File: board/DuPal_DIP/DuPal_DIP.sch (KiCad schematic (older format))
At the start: 45 parts, among them J1 AVR-ISP-6, J2 RS232, J3 Power IN, SW1 SW_Push, SW2 Power, U1 ATmega8A-PU, U2 74HC595, U3 74HC595, U5 20 Pin PAL, U6 MAX232, U7 L7805, Y1 8Mhz

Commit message: Begin connecting the new ICs in the circuit
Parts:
- removed U?: FT232RL, Package_SO:SSOP-28_5.3x10.2mm_P0.65mm, symbol Interface_USB:FT232RL
- added C? (x3): 100nF, Capacitor_THT:C_Disc_D3.4mm_W2.1mm_P2.50mm, symbol Device:C_Small
- added D?: PAL24_LED, LED_THT:LED_D2.0mm_W4.8mm_H2.5mm_FlatTop, symbol Device:LED_Small
- added D?: PAL20_LED, LED_THT:LED_D2.0mm_W4.8mm_H2.5mm_FlatTop, symbol Device:LED_Small
- added R? (x2): 680, Resistor_THT:R_Axial_DIN0204_L3.6mm_D1.6mm_P7.62mm_Horizontal, symbol Device:R_Small
- R16: value 470 -> 680
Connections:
- net labels added: PISO_I_1, PISO_I_10, PISO_I_11, PISO_I_12, PISO_I_13, PISO_I_14, PISO_I_15, PISO_I_16, PISO_I_2, PISO_I_3, PISO_I_4, PISO_I_5, PISO_I_6, PISO_I_7, PISO_I_8, PISO_I_9
- wire segments 298 -> 324
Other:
- moved on the sheet: C10, C11, C12, C8, C9, R1, R2, R3, R4, R5, R6, R7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

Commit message: Add 24 pin slot
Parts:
- added U?: 24 Pin PAL, symbol Logic_Programmable:PAL20L8
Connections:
- net labels added: P24_1, P24_10, P24_11, P24_13, P24_14, P24_15, P24_16, P24_17, P24_18, P24_19, P24_2, P24_20, P24_21, P24_22, P24_23, P24_3, P24_4, P24_5, P24_6, P24_7, P24_8, P24_9
- wire segments 324 -> 348
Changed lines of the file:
@@
 L Logic_Programmable:PAL16L8 U5
 U 1 1 5E5512FA
-P 6700 1650
-F 0 "U5" H 6400 2250 50  0000 C CNN
-F 1 "20 Pin PAL" H 6950 2250 50  0000 C CNN
-F 2 "Socket:DIP_Socket-20_W4.3_W5.08_W7.62_W10.16_W10.9_3M_220-3342-00-0602J" H 6700 1650 50  0001 C CNN
-F 3 "" H 6700 1650 50  0001 C CNN
-	1    6700 1650
+P 6300 1550
+F 0 "U5" H 6000 2150 50  0000 C CNN
+F 1 "20 Pin PAL" H 6550 2150 50  0000 C CNN
+F 2 "Socket:DIP_Socket-20_W4.3_W5.08_W7.62_W10.16_W10.9_3M_220-3342-00-0602J" H 6300 1550 50  0001 C CNN
+F 3 "" H 6300 1550 50  0001 C CNN
+	1    6300 1550
 	1    0    0    -1
 $EndComp
@@
 L power:GND #PWR0104
 U 1 1 5E551F7F
-P 6700 2300
-F 0 "#PWR0104" H 6700 2050 50  0001 C CNN
-F 1 "GND" H 6705 2127 50  0000 C CNN
-F 2 "" H 6700 2300 50  0001 C CNN
-F 3 "" H 6700 2300 50  0001 C CNN
-	1    6700 2300
-	1    0    0    -1
-$EndComp
-Wire Wire Line
-	6700 2300 6700 2250
+P 6300 2200
+F 0 "#PWR0104" H 6300 1950 50  0001 C CNN
+F 1 "GND" H 6305 2027 50  0000 C CNN
+F 2 "" H 6300 2200 50  0001 C CNN
+F 3 "" H 6300 2200 50  0001 C CNN
+	1    6300 2200
+	1    0    0    -1
+$EndComp
+Wire Wire Line
+	6300 2200 6300 2150
 $Comp
 L power:VCC #PWR0105
 U 1 1 5E5538C6
-P 6700 900
-F 0 "#PWR0105" H 6700 750 50  0001 C CNN
-F 1 "VCC" H 6717 1073 50  0000 C CNN
-F 2 "" H 6700 900 50  0001 C CNN
-F 3 "" H 6700 900 50  0001 C CNN
-	1    6700 900
-	1    0    0    -1
-$EndComp
-Wire Wire Line
-	6700 900  6700 950
+P 6300 800
+F 0 "#PWR0105" H 6300 650 50  0001 C CNN
+F 1 "VCC" H 6317 973 50  0000 C CNN
+F 2 "" H 6300 800 50  0001 C CNN
+F 3 "" H 6300 800 50  0001 C CNN
+	1    6300 800
+	1    0    0    -1
+$EndComp
+Wire Wire Line
+	6300 800  6300 850
 $Comp
 L power:VCC #PWR0106
@@
 P20_19
 Wire Wire Line
-	6200 1150 5750 1150
-Wire Wire Line
-	6200 1250 5750 1250
-Wire Wire Line
-	6200 1350 5750 1350
-Wire Wire Line
-	6200 1450 5750 1450
-Wire Wire Line
-	6200 1550 5750 1550
-Wire Wire Line
-	6200 1650 5750 1650
-Wire Wire Line
-	6200 1750 5750 1750
-Wire Wire Line
-	6200 1850 5750 1850
-Wire Wire Line
-	6200 1950 5750 1950
-Wire Wire Line
-	6200 2050 5750 2050
-Wire Wire Line
-	7200 1150 7800 1150
-Wire Wire Line
-	7200 1250 7800 1250
-Wire Wire Line
-	7200 1350 7800 1350
-Wire Wire Line
-	7200 1450 7800 1450
-Wire Wire Line
-	7200 1550 7800 1550
-Wire Wire Line
-	7200 1650 7800 1650
-Wire Wire Line
-	7200 1750 7800 1750
-Wire Wire Line
-	7200 1850 7800 1850
-Text Label 5750 1150 0    50   ~ 0
+	5800 1050 5350 1050
+Wire Wire Line
+	5800 1150 5350 1150
+Wire Wire Line
+	5800 1250 5350 1250
+Wire Wire Line
+	5800 1350 5350 1350
+Wire Wire Line
+	5800 1450 5350 1450
+Wire Wire Line
+	5800 1550 5350 1550
+Wire Wire Line
+	5800 1650 5350 1650
+Wire Wire Line
+	5800 1750 5350 1750
+Wire Wire Line
+	5800 1850 5350 1850
+Wire Wire Line
+	5800 1950 5350 1950
+Wire Wire Line
+	6800 1050 7400 1050
+Wire Wire Line
+	6800 1150 7400 1150
+Wire Wire Line
+	6800 1250 7400 1250
+Wire Wire Line
+	6800 1350 7400 1350
+Wire Wire Line
+	6800 1450 7400 1450
+Wire Wire Line
+	6800 1550 7400 1550
+Wire Wire Line
+	6800 1650 7400 1650
+Wire Wire Line
+	6800 1750 7400 1750
+Text Label 5350 1050 0    50   ~ 0
 P20_1
-Text Label 5750 1250 0    50   ~ 0
+Text Label 5350 1150 0    50   ~ 0
 P20_2
-Text Label 5750 1350 0    50   ~ 0
+Text Label 5350 1250 0    50   ~ 0
 P20_3
-Text Label 5750 1450 0    50   ~ 0
+Text Label 5350 1350 0    50   ~ 0
 P20_4
-Text Label 5750 1550 0    50   ~ 0
+Text Label 5350 1450 0    50   ~ 0
 P20_5
-Text Label 5750 1650 0    50   ~ 0
+Text Label 5350 1550 0    50   ~ 0
 P20_6
-Text Label 5750 1750 0    50   ~ 0
+Text Label 5350 1650 0    50   ~ 0
 P20_7
-Text Label 5750 1850 0    50   ~ 0
+Text Label 5350 1750 0    50   ~ 0
 P20_8
-Text Label 5750 1950 0    50   ~ 0
+Text Label 5350 1850 0    50   ~ 0
 P20_9
-Text Label 5750 2050 0    50   ~ 0
+Text Label 5350 1950 0    50   ~ 0
 P20_11
-Text Label 7800 1850 2    50   ~ 0
+Text Label 7400 1750 2    50   ~ 0
 P20_12
-Text Label 7800 1750 2    50   ~ 0
+Text Label 7400 1650 2    50   ~ 0
 P20_13
-Text Label 7800 1650 2    50   ~ 0
+Text Label 7400 1550 2    50   ~ 0
 P20_14
-Text Label 7800 1550 2    50   ~ 0
+Text Label 7400 1450 2    50   ~ 0
 P20_15
-Text Label 7800 1450 2    50   ~ 0
+Text Label 7400 1350 2    50   ~ 0
 P20_16
-Text Label 7800 1350 2    50   ~ 0
+Text Label 7400 1250 2    50   ~ 0
 P20_17
-Text Label 7800 1250 2    50   ~ 0
+Text Label 7400 1150 2    50   ~ 0
 P20_18
-Text Label 7800 1150 2    50   ~ 0
+Text Label 7400 1050 2    50   ~ 0
 P20_19
 NoConn ~ 14350 5800
@@
 Wire Wire Line
 	4150 2550 4150 2600
+$Comp
+L Logic_Programmable:PAL20L8 U?
+U 1 1 61C8AE16
+P 8500 1750
+F 0 "U?" H 8200 2550 50  0000 C CNN
+F 1 "24 Pin PAL" H 8750 2550 50  0000 C CNN
+F 2 "" H 8500 1750 50  0001 C CNN
+F 3 "" H 8500 1750 50  0001 C CNN
+	1    8500 1750
+	1    0    0    -1
+$EndComp
+$Comp
+L power:VCC #PWR?
+U 1 1 61D2E65D
+P 8500 800
+F 0 "#PWR?" H 8500 650 50  0001 C CNN
+F 1 "VCC" H 8517 973 50  0000 C CNN
+F 2 "" H 8500 800 50  0001 C CNN
+F 3 "" H 8500 800 50  0001 C CNN
+	1    8500 800
+	1    0    0    -1
+$EndComp
+Wire Wire Line
+	8500 800  8500 850
+$Comp
+L power:GND #PWR?
+U 1 1 61D50A38
+P 8500 2600
+F 0 "#PWR?" H 8500 2350 50  0001 C CNN
+F 1 "GND" H 8505 2427 50  0000 C CNN
+F 2 "" H 8500 2600 50  0001 C CNN
+F 3 "" H 8500 2600 50  0001 C CNN
+	1    8500 2600
+	1    0    0    -1
+$EndComp
+Wire Wire Line
+	8500 2550 8500 2600
+Wire Wire Line
+	8000 1050 7600 1050
+Wire Wire Line
+	8000 1150 7600 1150
+Wire Wire Line
+	8000 1250 7600 1250
+Wire Wire Line
+	8000 1350 7600 1350
+Wire Wire Line
+	8000 1450 7600 1450
+Wire Wire Line
+	8000 1550 7600 1550
+Wire Wire Line
+	8000 1650 7600 1650
+Wire Wire Line
+	8000 1750 7600 1750
+Wire Wire Line
+	8000 1850 7600 1850
+Wire Wire Line
+	8000 1950 7600 1950
+Wire Wire Line
+	8000 2050 7600 2050
+Wire Wire Line
+	8000 2150 7600 2150
+Wire Wire Line
+	8000 2250 7600 2250
+Wire Wire Line
+	8000 2350 7600 2350
+Wire Wire Line
+	9000 1050 9400 1050
+Wire Wire Line
+	9000 1150 9400 1150
+Wire Wire Line
+	9000 1250 9400 1250
+Wire Wire Line
+	9000 1350 9400 1350
+Wire Wire Line
+	9000 1450 9400 1450
+Wire Wire Line
+	9000 1550 9400 1550
+Wire Wire Line
+	9000 1650 9400 1650
+Wire Wire Line
+	9000 1750 9400 1750
+Text Label 7600 1050 0    50   ~ 0
+P24_1
+Text Label 7600 1150 0    50   ~ 0
+P24_2
+Text Label 7600 1250 0    50   ~ 0
+P24_3
+Text Label 7600 1350 0    50   ~ 0
+P24_4
+Text Label 7600 1450 0    50   ~ 0
+P24_5
+Text Label 7600 1550 0    50   ~ 0
+P24_6
+Text Label 7600 1650 0    50   ~ 0
+P24_7
+Text Label 7600 1750 0    50   ~ 0
+P24_8
+Text Label 7600 1850 0    50   ~ 0
+P24_9
+Text Label 7600 1950 0    50   ~ 0
+P24_10
+Text Label 7600 2050 0    50   ~ 0
+P24_11
+Text Label 7600 2150 0    50   ~ 0
+P24_13
+Text Label 7600 2250 0    50   ~ 0
+P24_14
+Text Label 7600 2350 0    50   ~ 0
+P24_23
+Text Label 9400 1750 2    50   ~ 0
+P24_15
+Text Label 9400 1650 2    50   ~ 0
+P24_16
+Text Label 9400 1550 2    50   ~ 0
+P24_17
+Text Label 9400 1450 2    50   ~ 0
+P24_18
+Text Label 9400 1350 2    50   ~ 0
+P24_19
+Text Label 9400 1250 2    50   ~ 0
+P24_20
+Text Label 9400 1150 2    50   ~ 0
+P24_21
+Text Label 9400 1050 2    50   ~ 0
+P24_22
 $EndSCHEMATC

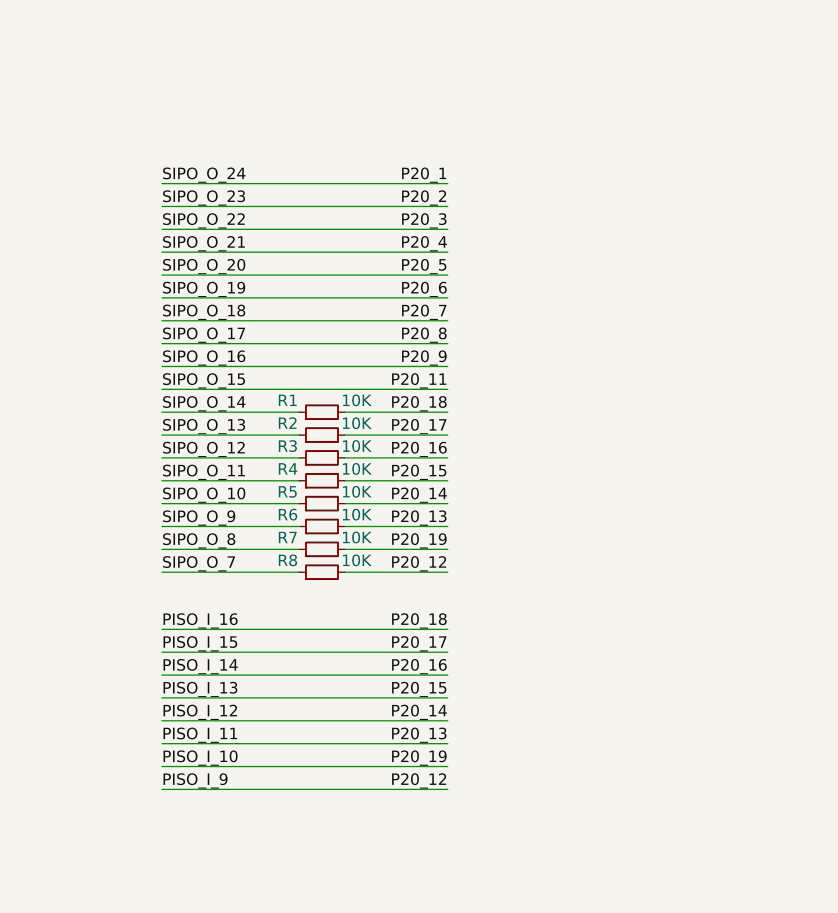
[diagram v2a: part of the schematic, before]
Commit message: Connected both PAL outputs
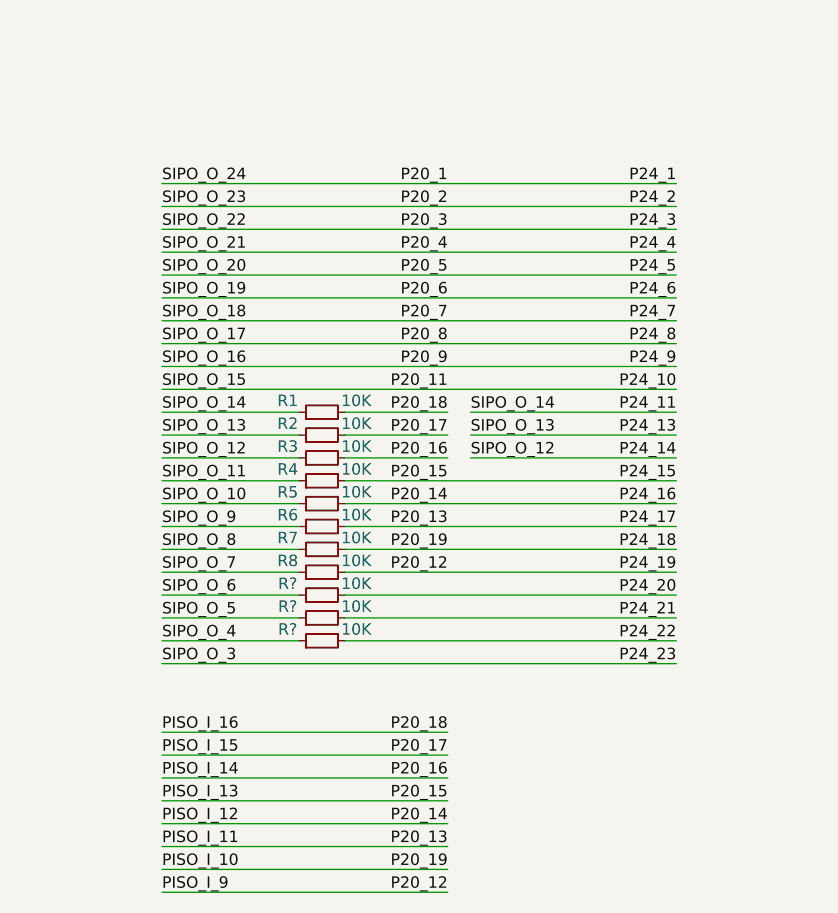
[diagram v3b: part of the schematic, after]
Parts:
- added R? (x3): 10K, Resistor_THT:R_Axial_DIN0204_L3.6mm_D1.6mm_P7.62mm_Horizontal, symbol Device:R_Small
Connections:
- wire segments 348 -> 358
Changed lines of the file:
@@
 Text Label 12500 5350 2    50   ~ 0
 PISO_SER
-Wire Wire Line
-	8500 6350 9750 6350
-Wire Wire Line
-	8500 6450 9750 6450
-Wire Wire Line
-	8500 6550 9750 6550
-Wire Wire Line
-	8500 6650 9750 6650
-Wire Wire Line
-	8500 6750 9750 6750
-Wire Wire Line
-	8500 6850 9750 6850
-Wire Wire Line
-	8500 6950 9750 6950
-Wire Wire Line
-	8500 7050 9750 7050
-Wire Wire Line
-	8500 7150 9750 7150
-Wire Wire Line
-	8500 7250 9750 7250
 Text Label 9750 6350 2    50   ~ 0
 P20_1
@@
 	9300 7550 9750 7550
 Wire Wire Line
-	9300 7650 9750 7650
-Wire Wire Line
-	9300 7750 9750 7750
-Wire Wire Line
-	9300 7850 9750 7850
-Wire Wire Line
-	9300 7950 9750 7950
-Wire Wire Line
-	9300 8050 9750 8050
-Wire Wire Line
 	8500 7350 9100 7350
 Wire Wire Line
@@
 PISO_I_16
 Wire Wire Line
-	8500 8300 9750 8300
-Wire Wire Line
-	8500 8400 9750 8400
-Wire Wire Line
-	8500 8500 9750 8500
-Wire Wire Line
-	8500 8600 9750 8600
-Wire Wire Line
-	8500 8700 9750 8700
-Wire Wire Line
-	8500 8800 9750 8800
-Wire Wire Line
-	8500 8900 9750 8900
-Wire Wire Line
-	8500 9000 9750 9000
-Text Label 9750 8900 2    50   ~ 0
+	8500 8750 9750 8750
+Wire Wire Line
+	8500 8850 9750 8850
+Wire Wire Line
+	8500 8950 9750 8950
+Wire Wire Line
+	8500 9050 9750 9050
+Wire Wire Line
+	8500 9150 9750 9150
+Wire Wire Line
+	8500 9250 9750 9250
+Wire Wire Line
+	8500 9350 9750 9350
+Wire Wire Line
+	8500 9450 9750 9450
+Text Label 9750 9350 2    50   ~ 0
 P20_19
-Text Label 9750 9000 2    50   ~ 0
+Text Label 9750 9450 2    50   ~ 0
 P20_12
-Text Label 9750 8800 2    50   ~ 0
+Text Label 9750 9250 2    50   ~ 0
 P20_13
-Text Label 9750 8700 2    50   ~ 0
+Text Label 9750 9150 2    50   ~ 0
 P20_14
-Text Label 9750 8600 2    50   ~ 0
+Text Label 9750 9050 2    50   ~ 0
 P20_15
-Text Label 9750 8500 2    50   ~ 0
+Text Label 9750 8950 2    50   ~ 0
 P20_16
-Text Label 9750 8400 2    50   ~ 0
+Text Label 9750 8850 2    50   ~ 0
 P20_17
-Text Label 9750 8300 2    50   ~ 0
+Text Label 9750 8750 2    50   ~ 0
 P20_18
-Text Label 8500 8300 0    50   ~ 0
+Text Label 8500 8750 0    50   ~ 0
 PISO_I_16
-Text Label 8500 8400 0    50   ~ 0
+Text Label 8500 8850 0    50   ~ 0
 PISO_I_15
-Text Label 8500 8500 0    50   ~ 0
+Text Label 8500 8950 0    50   ~ 0
 PISO_I_14
-Text Label 8500 8600 0    50   ~ 0
+Text Label 8500 9050 0    50   ~ 0
 PISO_I_13
-Text Label 8500 8700 0    50   ~ 0
+Text Label 8500 9150 0    50   ~ 0
 PISO_I_12
-Text Label 8500 8800 0    50   ~ 0
+Text Label 8500 9250 0    50   ~ 0
 PISO_I_11
-Text Label 8500 8900 0    50   ~ 0
+Text Label 8500 9350 0    50   ~ 0
 PISO_I_10
-Text Label 8500 9000 0    50   ~ 0
+Text Label 8500 9450 0    50   ~ 0
 PISO_I_9
 Wire Wire Line
@@
 Text Label 9400 1050 2    50   ~ 0
 P24_22
+Wire Wire Line
+	8500 6350 10750 6350
+Text Label 10750 6350 2    50   ~ 0
+P24_1
+Wire Wire Line
+	8500 6450 10750 6450
+Wire Wire Line
+	8500 6550 10750 6550
+Wire Wire Line
+	8500 6650 10750 6650
+Wire Wire Line
+	8500 6750 10750 6750
+Wire Wire Line
+	8500 6850 10750 6850
+Wire Wire Line
+	8500 6950 10750 6950
+Wire Wire Line
+	8500 7050 10750 7050
+Wire Wire Line
+	8500 7150 10750 7150
+Text Label 10750 6450 2    50   ~ 0
+P24_2
+Text Label 10750 6550 2    50   ~ 0
+P24_3
+Text Label 10750 6650 2    50   ~ 0
+P24_4
+Text Label 10750 6750 2    50   ~ 0
+P24_5
+Text Label 10750 6850 2    50   ~ 0
+P24_6
+Text Label 10750 6950 2    50   ~ 0
+P24_7
+Text Label 10750 7050 2    50   ~ 0
+P24_8
+Text Label 10750 7150 2    50   ~ 0
+P24_9
+Wire Wire Line
+	8500 7250 10750 7250
+Text Label 10750 7250 2    50   ~ 0
+P24_10
+Wire Wire Line
+	9850 7350 10750 7350
+Text Label 10750 7350 2    50   ~ 0
+P24_11
+Text Label 9850 7350 0    50   ~ 0
+SIPO_O_14
+Wire Wire Line
+	9850 7450 10750 7450
+Text Label 9850 7450 0    50   ~ 0
+SIPO_O_13
+Text Label 10750 7450 2    50   ~ 0
+P24_13
+Wire Wire Line
+	9850 7550 10750 7550
+Text Label 10750 7550 2    50   ~ 0
+P24_14
+Text Label 9850 7550 0    50   ~ 0
+SIPO_O_12
+Wire Wire Line
+	9300 7750 10750 7750
+Wire Wire Line
+	9300 7850 10750 7850
+Wire Wire Line
+	9300 7950 10750 7950
+Wire Wire Line
+	9300 8050 10750 8050
+Wire Wire Line
+	9300 7650 10750 7650
+Text Label 10750 7650 2    50   ~ 0
+P24_15
+Text Label 10750 7750 2    50   ~ 0
+P24_16
+Text Label 10750 7850 2    50   ~ 0
+P24_17
+Text Label 10750 7950 2    50   ~ 0
+P24_18
+Text Label 10750 8050 2    50   ~ 0
+P24_19
+$Comp
+L Device:R_Small R?
+U 1 1 6281CDD0
+P 9200 8150
+F 0 "R?" V 9250 8300 50  0000 C CNN
+F 1 "10K" V 9250 8000 50  0000 C CNN
+F 2 "Resistor_THT:R_Axial_DIN0204_L3.6mm_D1.6mm_P7.62mm_Horizontal" H 9200 8150 50  0001 C CNN
+F 3 "~" H 9200 8150 50  0001 C CNN
+	1    9200 8150
+	0    -1   -1   0
+$EndComp
+$Comp
+L Device:R_Small R?
+U 1 1 6281D384
+P 9200 8250
+F 0 "R?" V 9250 8400 50  0000 C CNN
+F 1 "10K" V 9250 8100 50  0000 C CNN
+F 2 "Resistor_THT:R_Axial_DIN0204_L3.6mm_D1.6mm_P7.62mm_Horizontal" H 9200 8250 50  0001 C CNN
+F 3 "~" H 9200 8250 50  0001 C CNN
+	1    9200 8250
+	0    -1   -1   0
+$EndComp
+$Comp
+L Device:R_Small R?
+U 1 1 6281D9F7
+P 9200 8350
+F 0 "R?" V 9250 8500 50  0000 C CNN
+F 1 "10K" V 9250 8200 50  0000 C CNN
+F 2 "Resistor_THT:R_Axial_DIN0204_L3.6mm_D1.6mm_P7.62mm_Horizontal" H 9200 8350 50  0001 C CNN
+F 3 "~" H 9200 8350 50  0001 C CNN
+	1    9200 8350
+	0    -1   -1   0
+$EndComp
+Wire Wire Line
+	9100 8150 8500 8150
+Wire Wire Line
+	9100 8250 8500 8250
+Wire Wire Line
+	9100 8350 8500 8350
+Wire Wire Line
+	8500 8450 10750 8450
+Wire Wire Line
+	9300 8150 10750 8150
+Wire Wire Line
+	9300 8250 10750 8250
+Wire Wire Line
+	9300 8350 10750 8350
+Text Label 8500 8150 0    50   ~ 0
+SIPO_O_6
+Text Label 8500 8250 0    50   ~ 0
+SIPO_O_5
+Text Label 8500 8350 0    50   ~ 0
+SIPO_O_4
+Text Label 8500 8450 0    50   ~ 0
+SIPO_O_3
+Text Label 10750 8150 2    50   ~ 0
+P24_20
+Text Label 10750 8250 2    50   ~ 0
+P24_21
+Text Label 10750 8350 2    50   ~ 0
+P24_22
+Text Label 10750 8450 2    50   ~ 0
+P24_23
 $EndSCHEMATC

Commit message: Reworked the outputs and added the inputs to the new PAL
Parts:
- removed R? (x3): 10K, Resistor_THT:R_Axial_DIN0204_L3.6mm_D1.6mm_P7.62mm_Horizontal, symbol Device:R_Small
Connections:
- wire segments 358 -> 352
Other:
- moved on the sheet: R1, R2, R3, R4, R5, R6, R7, R8

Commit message: Cleanup schematics, removed unused IC
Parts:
- removed U?: 74HC166, symbol 74xx_IEEE:74166
- added H1, H2, H3, H4: MountingHole_Pad, symbol Mechanical:MountingHole_Pad
- U10: renamed from U?; footprint (none) -> Socket:DIP_Socket-24_W4.3_W5.08_W7.62_W10.16_W10.9_3M_224-5248-00-0602J
- U8: renamed from U?; footprint (none) -> Package_DIP:DIP-16_W7.62mm
- gave numbers to parts that had none: 4
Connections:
- net labels removed: PISO_I_10, PISO_I_11, PISO_I_12, PISO_I_13, PISO_I_14, PISO_I_15, PISO_I_16, PISO_I_9
- wire segments 352 -> 325
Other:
- moved on the sheet: C10, C11, C12, C13, C14, C15, C8, C9

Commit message: Assign more footprints and names
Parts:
- gave numbers to parts that had none: 4
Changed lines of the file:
@@
 $EndComp
 $Comp
-L power:VCC #PWR?
+L power:VCC #PWR0127
 U 1 1 5F3CD87E
 P 13850 4650
-F 0 "#PWR?" H 13850 4500 50  0001 C CNN
+F 0 "#PWR0127" H 13850 4500 50  0001 C CNN
 F 1 "VCC" H 13867 4823 50  0000 C CNN
 F 2 "" H 13850 4650 50  0001 C CNN
@@
 	13150 5100 13450 5100
 $Comp
-L power:GND #PWR?
+L power:GND #PWR0128
 U 1 1 5F3CD895
 P 13850 6050
-F 0 "#PWR?" H 13850 5800 50  0001 C CNN
+F 0 "#PWR0128" H 13850 5800 50  0001 C CNN
 F 1 "GND" H 13855 5877 50  0000 C CNN
 F 2 "" H 13850 6050 50  0001 C CNN
@@
 $EndComp
 $Comp
-L power:VCC #PWR?
+L power:VCC #PWR0129
 U 1 1 5F56E5A8
 P 11650 1400
-F 0 "#PWR?" H 11650 1250 50  0001 C CNN
+F 0 "#PWR0129" H 11650 1250 50  0001 C CNN
 F 1 "VCC" H 11667 1573 50  0000 C CNN
 F 2 "" H 11650 1400 50  0001 C CNN
@@
 $EndComp
 $Comp
-L power:GND #PWR?
+L power:GND #PWR0130
 U 1 1 5F56EF46
 P 11500 1400
-F 0 "#PWR?" H 11500 1150 50  0001 C CNN
+F 0 "#PWR0130" H 11500 1150 50  0001 C CNN
 F 1 "GND" H 11505 1227 50  0000 C CNN
 F 2 "" H 11500 1400 50  0001 C CNN
@@
 	12000 2950 12500 2950
 $Comp
-L power:GND #PWR?
+L power:GND #PWR0131
 U 1 1 5F729F7E
 P 10450 2150
-F 0 "#PWR?" H 10450 1900 50  0001 C CNN
+F 0 "#PWR0131" H 10450 1900 50  0001 C CNN
 F 1 "GND" H 10455 1977 50  0000 C CNN
 F 2 "" H 10450 2150 50  0001 C CNN
@@
 	4050 1900 4150 1900
 $Comp
-L Device:LED_Small D?
+L Device:LED_Small D5
 U 1 1 61B70AE6
 P 3650 2600
-F 0 "D?" H 3650 2400 50  0000 C CNN
+F 0 "D5" H 3650 2400 50  0000 C CNN
 F 1 "PAL24_LED" H 3650 2500 50  0000 C CNN
 F 2 "LED_THT:LED_D2.0mm_W4.8mm_H2.5mm_FlatTop" V 3650 2600 50  0001 C CNN
@@
 	2900 2600 3550 2600
 $Comp
-L Device:R_Small R?
+L Device:R_Small R20
 U 1 1 61B70AF1
 P 3950 2600
-F 0 "R?" V 3750 2600 50  0000 C CNN
+F 0 "R20" V 3750 2600 50  0000 C CNN
 F 1 "680" V 3850 2600 50  0000 C CNN
 F 2 "Resistor_THT:R_Axial_DIN0204_L3.6mm_D1.6mm_P7.62mm_Horizontal" H 3950 2600 50  0001 C CNN
@@
 	2900 2500 3550 2500
 $Comp
-L Device:R_Small R?
+L Device:R_Small R19
 U 1 1 61BC6E3A
 P 3950 2500
-F 0 "R?" V 4146 2500 50  0000 C CNN
+F 0 "R19" V 4146 2500 50  0000 C CNN
 F 1 "680" V 4055 2500 50  0000 C CNN
 F 2 "Resistor_THT:R_Axial_DIN0204_L3.6mm_D1.6mm_P7.62mm_Horizontal" H 3950 2500 50  0001 C CNN
@@
 	3850 2500 3750 2500
 $Comp
-L power:GND #PWR?
+L power:GND #PWR0132
 U 1 1 61BC6E45
 P 4200 2550
-F 0 "#PWR?" H 4200 2300 50  0001 C CNN
+F 0 "#PWR0132" H 4200 2300 50  0001 C CNN
 F 1 "GND" H 4205 2377 50  0000 C CNN
 F 2 "" H 4200 2550 50  0001 C CNN
@@
 	4050 2500 4150 2500
 $Comp
-L Device:LED_Small D?
+L Device:LED_Small D4
 U 1 1 61BC6E2F
 P 3650 2500
-F 0 "D?" H 3650 2750 50  0000 C CNN
+F 0 "D4" H 3650 2750 50  0000 C CNN
 F 1 "PAL20_LED" H 3650 2650 50  0000 C CNN
 F 2 "LED_THT:LED_D2.0mm_W4.8mm_H2.5mm_FlatTop" V 3650 2500 50  0001 C CNN
@@
 $EndComp
 $Comp
-L power:VCC #PWR?
+L power:VCC #PWR0133
 U 1 1 61D2E65D
 P 8500 800
-F 0 "#PWR?" H 8500 650 50  0001 C CNN
+F 0 "#PWR0133" H 8500 650 50  0001 C CNN
 F 1 "VCC" H 8517 973 50  0000 C CNN
 F 2 "" H 8500 800 50  0001 C CNN
@@
 	8500 800  8500 850
 $Comp
-L power:GND #PWR?
+L power:GND #PWR0134
 U 1 1 61D50A38
 P 8500 2600
-F 0 "#PWR?" H 8500 2350 50  0001 C CNN
+F 0 "#PWR0134" H 8500 2350 50  0001 C CNN
 F 1 "GND" H 8505 2427 50  0000 C CNN
 F 2 "" H 8500 2600 50  0001 C CNN
@@
 $EndComp
 $Comp
-L power:GND #PWR?
+L power:GND #PWR0135
 U 1 1 62ECCFAA
 P 5650 8850
-F 0 "#PWR?" H 5650 8600 50  0001 C CNN
+F 0 "#PWR0135" H 5650 8600 50  0001 C CNN
 F 1 "GND" H 5655 8677 50  0000 C CNN
 F 2 "" H 5650 8850 50  0001 C CNN
@@
 $EndComp
 $Comp
-L power:GND #PWR?
+L power:GND #PWR0136
 U 1 1 62EF4481
 P 6800 8850
-F 0 "#PWR?" H 6800 8600 50  0001 C CNN
+F 0 "#PWR0136" H 6800 8600 50  0001 C CNN
 F 1 "GND" H 6805 8677 50  0000 C CNN
 F 2 "" H 6800 8850 50  0001 C CNN
@@
 $EndComp
 $Comp
-L power:GND #PWR?
+L power:GND #PWR0137
 U 1 1 62F1CBCA
 P 5650 9650
-F 0 "#PWR?" H 5650 9400 50  0001 C CNN
+F 0 "#PWR0137" H 5650 9400 50  0001 C CNN
 F 1 "GND" H 5655 9477 50  0000 C CNN
 F 2 "" H 5650 9650 50  0001 C CNN
@@
 $EndComp
 $Comp
-L power:GND #PWR?
+L power:GND #PWR0138
 U 1 1 62F1CBDF
 P 6800 9650
-F 0 "#PWR?" H 6800 9400 50  0001 C CNN
+F 0 "#PWR0138" H 6800 9400 50  0001 C CNN
 F 1 "GND" H 6805 9477 50  0000 C CNN
 F 2 "" H 6800 9650 50  0001 C CNN
